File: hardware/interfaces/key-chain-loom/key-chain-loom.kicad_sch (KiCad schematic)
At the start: 11 parts

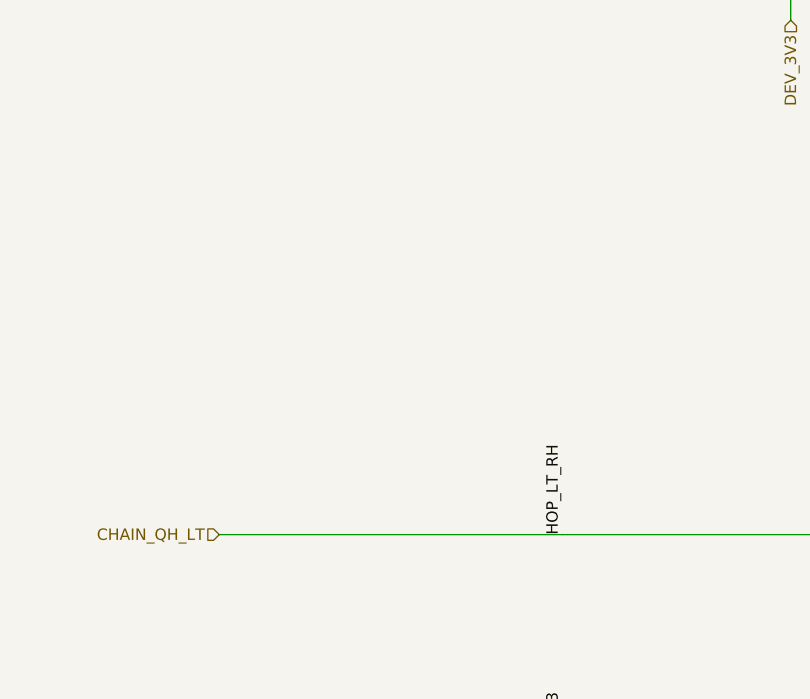
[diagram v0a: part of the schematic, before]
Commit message: Key chain: R-HOP-SER 2.2k at left_thumb's QH on the main board (A5-2)
Interface sheet and main-board root sheet (R44), exported and rendered; BOM row
(0603, JLC basic C4190); hop-hold-lt-to-rh now asserts the hop holds with zero
CLK->QH delay at every corner (hold margin 3.2-13.4 ns rising, 11.7-22.3 ns
falling); the old race kept as hop-hold-without-series-r. kicad.py holds the
new row in check_chain_main_parts. Pages, ADR 0001 amendment, nets.yaml.
Also guards power-entry/sim derived values for sims that import its params.

Co-Authored-By: Claude Opus 5.5 <noreply@anthropic.com>
Claude-Session: https://claude.ai/code/session_01LmB4muFXnoLprWX4JzuJ5A
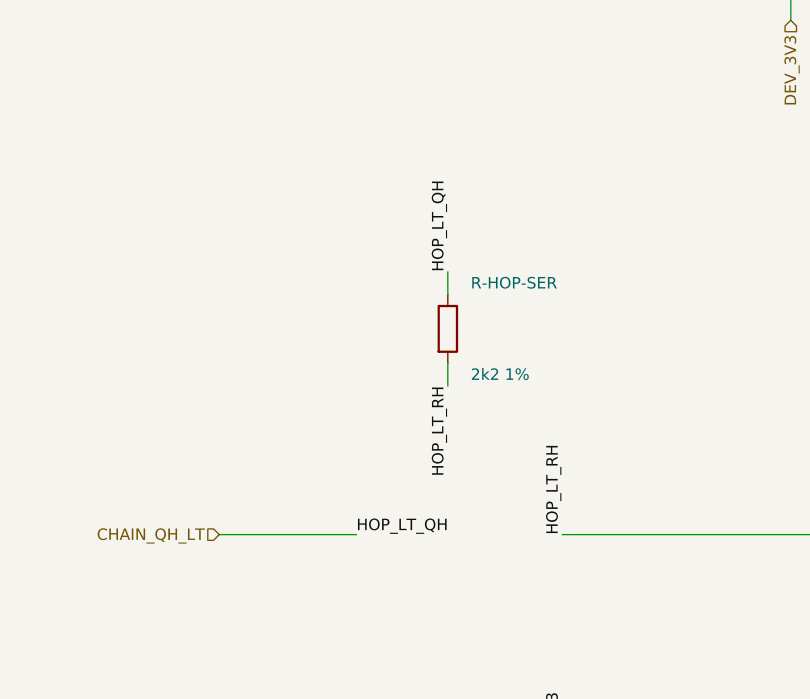
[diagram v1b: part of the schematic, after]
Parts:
- added R-HOP-SER: 2k2 1%, Resistor_SMD:R_0603_1608Metric, symbol Device:R
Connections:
- net CHAIN_QH_LT: now also R-HOP-SER.1; no longer J-CHAIN-KEY-RH.7 (Pin_7), J-CHAIN-MAIN-RH.6 (Pin_6)
- new net CHAIN_SER_RH: J-CHAIN-KEY-RH.7 (Pin_7), J-CHAIN-MAIN-RH.6 (Pin_6), R-HOP-SER.2
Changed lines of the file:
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@@
   (wire (pts (xy 63.5 228.6) (xy 101.6 228.6)) (stroke (width 0) (type default)))
   (wire (pts (xy 101.6 228.6) (xy 139.7 228.6)) (stroke (width 0) (type default)))
-  (wire (pts (xy 190.5 228.6) (xy 228.6 228.6)) (stroke (width 0) (type default)))
+  (wire (pts (xy 190.5 228.6) (xy 205.74 228.6)) (stroke (width 0) (type default)))
   (wire (pts (xy 228.6 228.6) (xy 266.7 228.6)) (stroke (width 0) (type default)))
   (wire (pts (xy 317.5 228.6) (xy 355.6 228.6)) (stroke (width 0) (type default)))
@@
     (property "Dir" "in" (at 190.5 228.6 0) (effects (font (size 1.27 1.27)) hide))
     (property "From" "cluster/key-register" (at 190.5 228.6 0) (effects (font (size 1.27 1.27)) hide)))
+  (label "HOP_LT_QH" (at 205.74 228.6 0) (fields_autoplaced) (effects (font (size 1.27 1.27)) (justify left bottom)))
   (label "HOP_LT_RH" (at 228.6 228.6 90) (fields_autoplaced) (effects (font (size 1.27 1.27)) (justify left bottom)))
   (hierarchical_label "CHAIN_SER_RH" (shape output) (at 266.7 228.6 0) (effects (font (size 1.27 1.27)) (justify left))
@@
   (text "Both ribbons, end to end. J-CHAIN-MAIN-RH/-LH, the series resistors, R-SER-TERM, the beads and U-TVS-CHAIN are on the MAIN board; J-CHAIN-KEY-RH and J-CHAIN-KEY-LH are each\nkey board's J-CHAIN. CBL-CHAIN is not a part: a main-board pin and the key-board pin its conductor reaches are one net. Which board carries which part: key-chain-loom.md,\n'Which board places what'. Below: the nets that carry two ports - a register's QH is the next register's SER - and CHAIN_QH_RT, which reaches no connector." (at 25.4 25.4 0) (effects (font (size 1.27 1.27)) (justify left top)))
   (text "FROM THE HAND-WRITTEN NETLIST THIS SHEET REPLACES (the part notes are on each part's Note field):\n\nAUTHORITATIVE for connectivity. The drawings on key-chain-loom.md are a REPRESENTATION of this file.\n\nTHE HOP MAP IS HERE, AS NETS. Chain order MCU <- RT <- RH <- LT <- LH (config/key-layout.yaml). right_thumb and left_thumb are on the main board; right_hand and left_hand are on the key boards, one\nIDC ribbon each. Each ribbon carries its key board's SER in on conductor 6 and its QH out on conductor 8, so every hop is a named net below.\n\nTHE REGISTER SIDE IS PER INSTANCE. cluster/key-register is one schematic built four times (`replicated: 4`) with generic CHAIN_SER / CHAIN_QH pins, so it cannot declare which instance sits on which\nhop. This file does, with one port per instance pin (CHAIN_SER_RT ... CHAIN_QH_LH), and hardware/nets.yaml marks those nets `per_board:` - the checker prints them rather than pretending the register\ndeclares them.\n\nTHE KEY-BOARD END NUMBERS THE CONDUCTORS DIFFERENTLY, AND THE CABLE SETS IT. Same 2x6 1.27 mm right-angle IDC header at both ends, the key board's mounted upside down on its underside, facing the same\nway. A keyed socket always mates position k to header pin k; CBL-CHAIN is ordered with its notch reversed on the key-board end (Samtec -RN2), so conductor k is main-board pin k and key-board pin 13-k\n[datasheet, both full prints banked; key-chain-loom.md].\n\nTHE CABLE IS NOT A COMPONENT HERE. CBL-CHAIN is a straight conductor per pin, so each ribbon is modelled as the nets it joins: a main-board pin and the key-board pin it reaches are on the same net.\n\nTHE CHAIN'S 3V3 IS DEV_3V3 ON THE MAIN BOARD, and each ribbon's conductor 10 is behind its own ferrite bead (ADR 0018). So V3V3_CHAIN - the name the replicated cluster schematics use - is the same\nnode as DEV_3V3 for the two registers on the main board, and each key board's rail is its own net past its bead (V3V3_CHAIN_RH, V3V3_CHAIN_LH), `per_board:` in hardware/nets.yaml like the hop nets.\nThere is no fuse: short-circuit protection is the Matrix LDO's own current limit (key-chain-loom.md).\n\n[CHAIN_SER_RT] one per register instance - see the header\n\n[CHAIN_SCK] One net each: right_thumb and left_thumb by trace, the key boards by ribbon.\n\n--- the hop map, from the chain end toward the MCU ------------------\n\n[CHAIN_SER_LH] Chain end: IO33 (or the pull-up) into left_hand's SER, over its ribbon.\n\n[HOP_LH_LT] left_hand's QH back over its ribbon into left_thumb's SER.\n\n[HOP_LT_RH] left_thumb's QH out over the right_hand ribbon into right_hand's SER.\n\n[HOP_RH_RT] right_hand's QH back over its ribbon into right_thumb's SER.\n\n[CHAIN_QH_RT] ONE NET, TWO BOUNDARIES: right_thumb's QH is a main-board trace to the MCU's pin. It reaches no connector, so the TVS is not on it.\n\n[DEV_3V3] ONE NET, TWO BOUNDARIES: the Matrix's 3V3 arriving from carrier/carrier, and the chain rail the main-board registers and R-SER-TERM sit on.\n\n[V3V3_CHAIN_RH] Each key board's rail, past its ribbon's bead.\n\n[CHAIN_SPARE_RH_11] ADR 0009's rule: two spare conductors per ribbon, end to end, unallocated." (at 25.4 279.4 0) (effects (font (size 1.27 1.27)) (justify left top)))
+  (symbol (lib_id "Device:R") (at 215.9 205.74 0) (unit 1)
+    (in_bom yes) (on_board yes) (dnp no)
+    (property "Reference" "R-HOP-SER" (at 218.44 200.66 0) (effects (font (size 1.27 1.27)) (justify left)))
+    (property "Value" "2k2 1%" (at 218.44 210.82000000000002 0) (effects (font (size 1.27 1.27)) (justify left)))
+    (property "Footprint" "Resistor_SMD:R_0603_1608Metric" (at 215.9 205.74 0) (effects (font (size 1.27 1.27)) hide))
+    (property "Datasheet" "" (at 215.9 205.74 0) (effects (font (size 1.27 1.27)) hide))
+    (property "Row" "R-HOP-SER" (at 215.9 205.74 0) (effects (font (size 1.27 1.27)) hide))
+    (property "Pins" "1=1 2=2" (at 215.9 205.74 0) (effects (font (size 1.27 1.27)) hide))
+    (property "Pins_source" "a two-terminal resistor; 1 at left_thumb's QH, 2 towards the ribbon" (at 215.9 205.74 0) (effects (font (size 1.27 1.27)) hide))
+    (property "Note" "At left_thumb's QH on the main board, before HOP_LT_RH leaves for the right_hand ribbon (owner, 2026-10-01; pre-layout review A5-2): its RC with the ribbon delays the hop's data past right_hand's clock, so the hop holds with no CLK-to-QH delay at all (key-chain-loom.md, The hop hold time; key-chain-loom/sim hop-hold-lt-to-rh)" (at 215.9 205.74 0) (effects (font (size 1.27 1.27)) hide))
+    (property "Manufacturer" "UNI-ROYAL" (at 215.9 205.74 0) (effects (font (size 1.27 1.27)) hide))
+    (property "MPN" "0603WAF2201T5E" (at 215.9 205.74 0) (effects (font (size 1.27 1.27)) hide))
+    (property "LCSC" "C4190" (at 215.9 205.74 0) (effects (font (size 1.27 1.27)) hide))
+    (property "Assembly" "machine" (at 215.9 205.74 0) (effects (font (size 1.27 1.27)) hide))
+    (pin "1")
+    (pin "2")
+    (instances (project "key-chain-loom" (path "/deca1880-f796-509a-b41b-fda81b07e63f" (reference "R-HOP-SER") (unit 1))))
+  )
+  (wire (pts (xy 215.9 201.93) (xy 215.9 199.39)) (stroke (width 0) (type default)))
+  (label "HOP_LT_QH" (at 215.9 199.39 90) (fields_autoplaced) (effects (font (size 1.27 1.27)) (justify left bottom)))
+  (wire (pts (xy 215.9 209.55) (xy 215.9 212.09)) (stroke (width 0) (type default)))
+  (label "HOP_LT_RH" (at 215.9 212.09 270) (fields_autoplaced) (effects (font (size 1.27 1.27)) (justify right bottom)))
   (sheet_instances (path "/" (page "1")))
 )

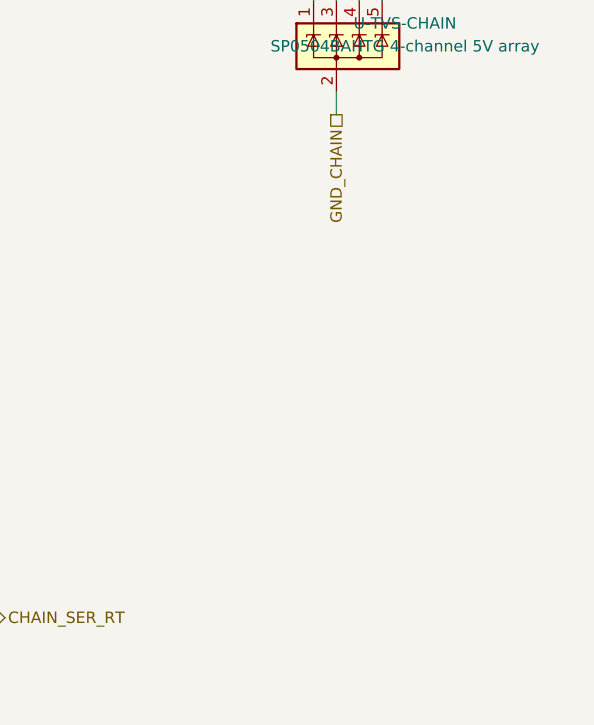
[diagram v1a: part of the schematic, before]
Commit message: Owner decisions D1, D2, D3, D5, CMRR: the parts on the sheets (#11, #14, #15, #16, #5, #12)
The owner's choices of 2026-10-03 (working chat), applied to the KiCad sheets,
exported, rendered, and carried into the BOM fragments:

- D1 (#11 F2, #14 A1, #12-3), "10 ohm + 22 uF + 10 uF": breath-adc gains
  R-ADC-VDD (10R 1% 0805, UNI-ROYAL 0805W8F100JT5E, C17415, JLC basic) from
  DEV_3V3 to a new local net ADC_VDD = U-ADC pin 8, with C-ADC-VDD (22 uF
  X5R 25 V 1206, Samsung CL31A226KAHNNNE, C12891, JLC basic) beside the
  existing C-ADC-BULK and C-DEC-ADC (C3 kept); a PWR_FLAG on ADC_VDD for
  ERC. power-entry-instrument gains C-BUCK-OUT (10 uF X5R 50 V 1206,
  Samsung CL31A106KBHNNNE, C13585, JLC basic) at U-BUCK-A's OUT (main-board
  U5, the R-78E5.0 - RECOM's standard application, #14 A1 item 3).
  Main board: R47, C42, C43.
- D5: U-ADC CH1 tied to AGND_INST.
- D2 (#15 C2, #16 B2), "Yes, all 4 channels": a second SP0504BAHTG at J5
  on CHAIN_SCK, CHAIN_SHLD, HOP_LT_RH, HOP_RH_RT - main-board U11 on the
  root sheet, U-TVS-CHAIN-RH on the key-chain-loom sheet; row qty 2.
- D3 (#15 C3): R-SPI-SER (R1-R3) Panasonic ERJ-P08F82R0V (C4065013, 0 at
  JLC and LCSC; in-stock equivalent Vishay CRCW120682R0FKEAHP, C1854869,
  named in the row); R-SER-BREATH-INST (R38/R39) ERJ-P08F1001V (C4261071,
  JLC 4,299).
- CMRR (#5-5), "Tighten cap matching": C-CM-BREATH a matched pair, each
  within 0.5 % of the pair's mean, from one reel of the 1 % C0G, measured
  and hand-fitted (no 1.5 nF C0G is catalogued tighter than 1 %).

Banked: Samsung CL31A226KAHNNNE and CL31A106KBHNNNE spec sheets, Vishay
CRCW-HP e3 (fragment .manifest-R51-owner-decisions.csv). Also two module
sims the deff676 merge staled and these changes do not touch (panel-led,
digital-and-supervision) re-run: 0 failed.

Gate-Red: sims staled by these netlists are re-running in the next commits; main-board .kicad_pcb awaits wave-3 placement of R47, C42, C43, U11 (and fab/ renders); known stale photos/clash

Co-Authored-By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
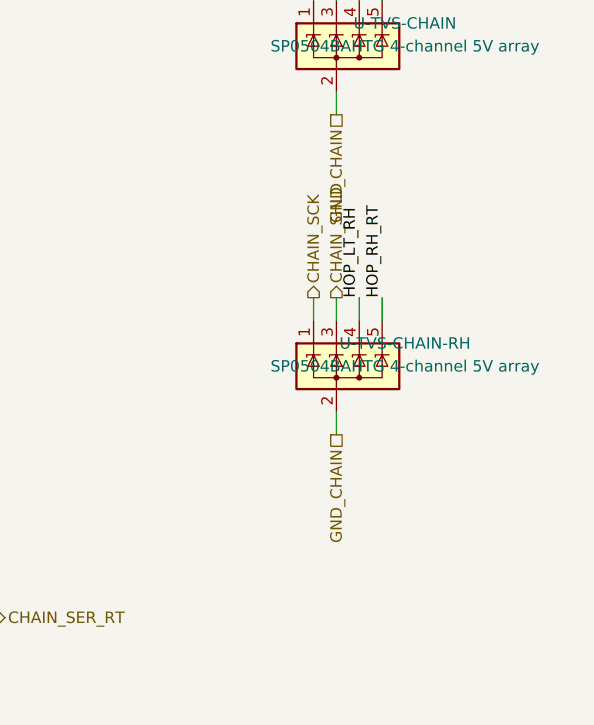
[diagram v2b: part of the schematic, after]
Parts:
- added U-TVS-CHAIN-RH: SP0504BAHTG 4-channel 5V array, Package_TO_SOT_SMD:SOT-23-5, symbol Power_Protection:SP0504BAHT
- U-TVS-CHAIN: Note FITTED (ADR 0018). On the three MCU nets the ribbon connectors expose, at the left_hand J-CHAIN. The fourth channel is spare -> FITTED (ADR 0018). On the three MCU nets the ribbon connectors expose, at the left_hand J-CHAIN (main board J4). The fourth channel is spare. U-TVS-CHAIN-RH guards the right_hand J-CHAIN (owner, 2026-10-03, D2)
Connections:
- net CHAIN_QH_RH: now also U-TVS-CHAIN-RH.5 (K)
- net CHAIN_SCK: now also U-TVS-CHAIN-RH.1 (K)
- net CHAIN_SER_RH: now also U-TVS-CHAIN-RH.4 (K)
- net CHAIN_SHLD: now also U-TVS-CHAIN-RH.3 (K)
- net GND_CHAIN: now also U-TVS-CHAIN-RH.2 (A)
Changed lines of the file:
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@@
     (property "Row" "U-TVS-CHAIN" (at 431.8 165.1 0) (effects (font (size 1.27 1.27)) hide))
     (property "Pins" "CH1=1(K) CH2=3(K) CH3=4(K) CH4=5(K) GND=2(A)" (at 431.8 165.1 0) (effects (font (size 1.27 1.27)) hide))
-    (property "Note" "FITTED (ADR 0018). On the three MCU nets the ribbon connectors expose, at the left_hand J-CHAIN. The fourth channel is spare" (at 431.8 165.1 0) (effects (font (size 1.27 1.27)) hide))
+    (property "Note" "FITTED (ADR 0018). On the three MCU nets the ribbon connectors expose, at the left_hand J-CHAIN (main board J4). The fourth channel is spare. U-TVS-CHAIN-RH guards the right_hand J-CHAIN (owner, 2026-10-03, D2)" (at 431.8 165.1 0) (effects (font (size 1.27 1.27)) hide))
     (property "Pins_source" "datasheets/discrete-and-power/SP0504BAHT.pdf p.1 pinout (SOT-23-5): I/O on 1, 3, 4, 5, ground on 2" (at 431.8 165.1 0) (effects (font (size 1.27 1.27)) hide))
     (property "Manufacturer" "Littelfuse" (at 431.8 165.1 0) (effects (font (size 1.27 1.27)) hide))
@@
   (wire (pts (xy 215.9 209.55) (xy 215.9 212.09)) (stroke (width 0) (type default)))
   (label "HOP_LT_RH" (at 215.9 212.09 270) (fields_autoplaced) (effects (font (size 1.27 1.27)) (justify right bottom)))
+  (symbol (lib_id "Power_Protection:SP0504BAHT") (at 431.8 200.66 0) (unit 1)
+    (in_bom yes) (on_board yes) (dnp no)
+    (property "Reference" "U-TVS-CHAIN-RH" (at 439.42 198.12 0) (effects (font (size 1.27 1.27))))
+    (property "Value" "SP0504BAHTG 4-channel 5V array" (at 439.42 200.66 0) (effects (font (size 1.27 1.27))))
+    (property "Footprint" "Package_TO_SOT_SMD:SOT-23-5" (at 439.42 201.93 0) (effects (font (size 1.27 1.27)) hide))
+    (property "Datasheet" "" (at 431.8 200.66 0) (effects (font (size 1.27 1.27)) hide))
+    (property "Row" "U-TVS-CHAIN" (at 431.8 200.66 0) (effects (font (size 1.27 1.27)) hide))
+    (property "Pins" "CH1=1(K) CH2=3(K) CH3=4(K) CH4=5(K) GND=2(A)" (at 431.8 200.66 0) (effects (font (size 1.27 1.27)) hide))
+    (property "Note" "FITTED (owner, 2026-10-03, D2: 'Yes, all 4 channels'). The second array, AT THE right_hand J-CHAIN (main board J5): CH1 CHAIN_SCK, CH2 CHAIN_SHLD, CH3 HOP_LT_RH, CH4 HOP_RH_RT, ground with a via at pin 2. J5 exposes the same two MCU pins J4 does, and U-TVS-CHAIN is at J4, a board's length away" (at 431.8 200.66 0) (effects (font (size 1.27 1.27)) hide))
+    (property "Pins_source" "datasheets/discrete-and-power/SP0504BAHT.pdf p.1 pinout (SOT-23-5): I/O on 1, 3, 4, 5, ground on 2" (at 431.8 200.66 0) (effects (font (size 1.27 1.27)) hide))
+    (property "Manufacturer" "Littelfuse" (at 431.8 200.66 0) (effects (font (size 1.27 1.27)) hide))
+    (property "MPN" "SP0504BAHTG" (at 431.8 200.66 0) (effects (font (size 1.27 1.27)) hide))
+    (property "LCSC" "C10675" (at 431.8 200.66 0) (effects (font (size 1.27 1.27)) hide))
+    (property "Assembly" "machine" (at 431.8 200.66 0) (effects (font (size 1.27 1.27)) hide))
+    (pin "2")
+    (pin "1")
+    (pin "3")
+    (pin "4")
+    (pin "5")
+    (instances (project "key-chain-loom" (path "/deca1880-f796-509a-b41b-fda81b07e63f" (reference "U-TVS-CHAIN-RH") (unit 1))))
+  )
+  (wire (pts (xy 429.26 195.58) (xy 429.26 193.04)) (stroke (width 0) (type default)))
+  (hierarchical_label "CHAIN_SCK" (shape output) (at 429.26 193.04 90) (effects (font (size 1.27 1.27)) (justify left))
+    (property "Dir" "out" (at 429.26 193.04 0) (effects (font (size 1.27 1.27)) hide))
+    (property "To" "cluster/key-register" (at 429.26 193.04 0) (effects (font (size 1.27 1.27)) hide))
+    (property "Figure" "chain-conductors" (at 429.26 193.04 0) (effects (font (size 1.27 1.27)) hide)))
+  (wire (pts (xy 431.8 195.58) (xy 431.8 193.04)) (stroke (width 0) (type default)))
+  (hierarchical_label "CHAIN_SHLD" (shape output) (at 431.8 193.04 90) (effects (font (size 1.27 1.27)) (justify left))
+    (property "Dir" "out" (at 431.8 193.04 0) (effects (font (size 1.27 1.27)) hide))
+    (property "To" "cluster/key-register" (at 431.8 193.04 0) (effects (font (size 1.27 1.27)) hide))
+    (property "Figure" "chain-conductors" (at 431.8 193.04 0) (effects (font (size 1.27 1.27)) hide)))
+  (wire (pts (xy 434.34 195.58) (xy 434.34 193.04)) (stroke (width 0) (type default)))
+  (label "HOP_LT_RH" (at 434.34 193.04 90) (fields_autoplaced) (effects (font (size 1.27 1.27)) (justify left bottom)))
+  (wire (pts (xy 436.88 195.58) (xy 436.88 193.04)) (stroke (width 0) (type default)))
+  (label "HOP_RH_RT" (at 436.88 193.04 90) (fields_autoplaced) (effects (font (size 1.27 1.27)) (justify left bottom)))
+  (wire (pts (xy 431.8 205.74) (xy 431.8 208.28)) (stroke (width 0) (type default)))
+  (hierarchical_label "GND_CHAIN" (shape passive) (at 431.8 208.28 270) (effects (font (size 1.27 1.27)) (justify right))
+    (property "Dir" "ref" (at 431.8 208.28 0) (effects (font (size 1.27 1.27)) hide))
+    (property "From" "interfaces/key-chain-loom" (at 431.8 208.28 0) (effects (font (size 1.27 1.27)) hide))
+    (property "Figure" "chain-conductors" (at 431.8 208.28 0) (effects (font (size 1.27 1.27)) hide)))
   (sheet_instances (path "/" (page "1")))
 )
